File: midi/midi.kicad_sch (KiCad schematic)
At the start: 36 parts, among them J1 Conn_01x02, J2 SJ-43515TS-SMT-TR, J3 USB_C_Receptacle_USB2.0_16P, U3 MAX98357A, U4 MAX98357A, U5 CD74HC154M96, U6 ESP32-S2-SOLO

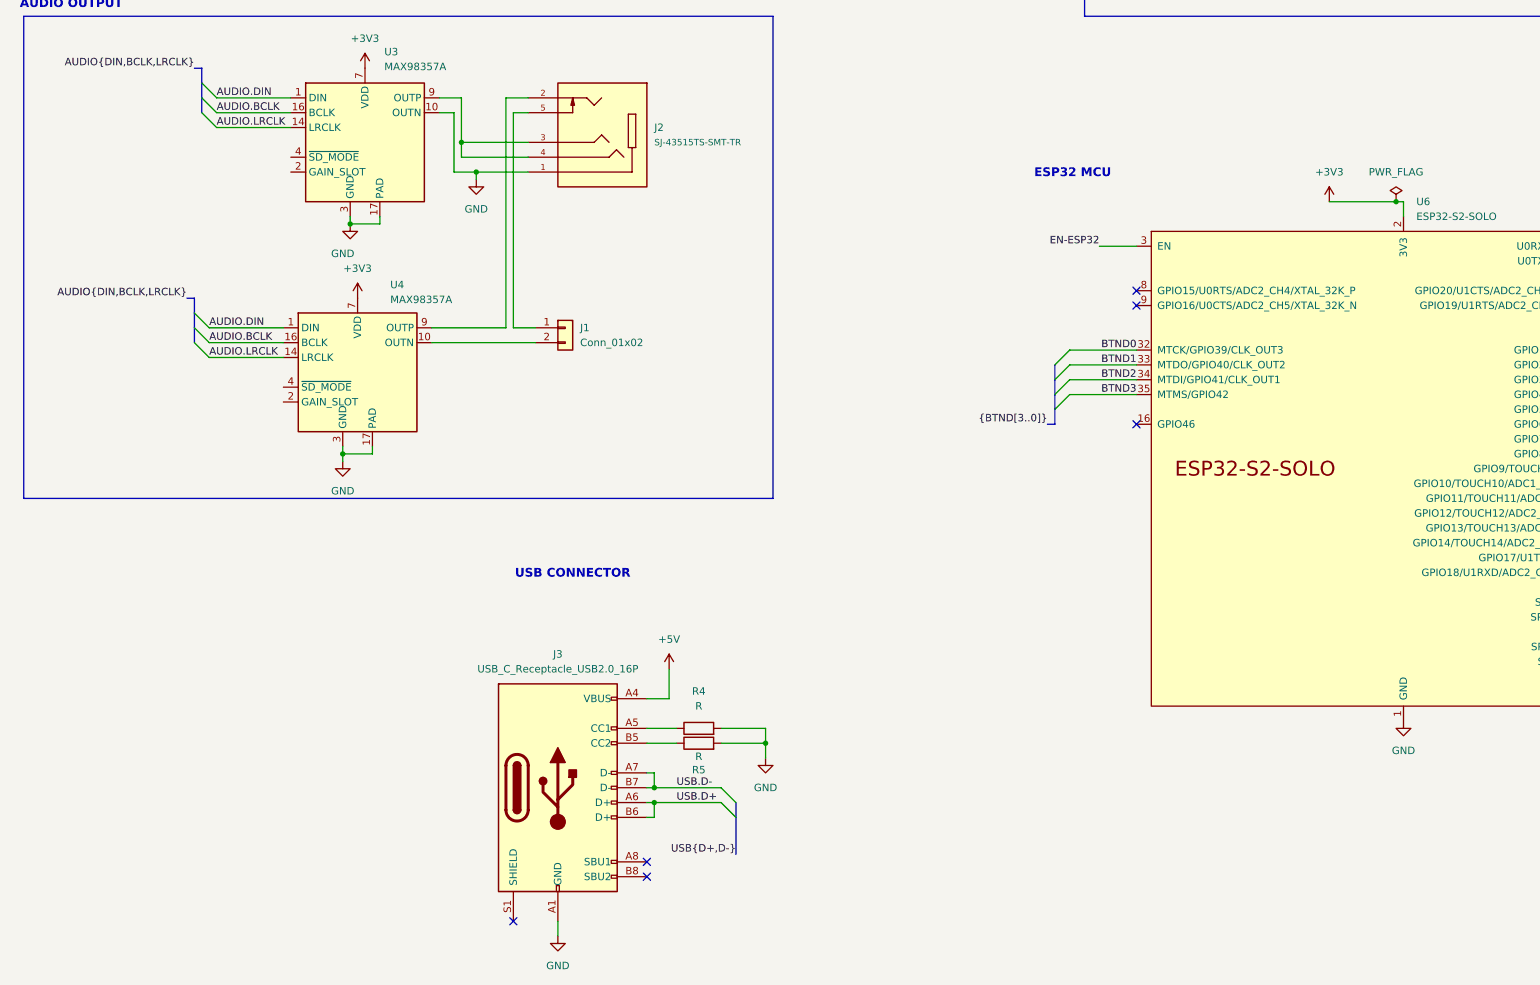
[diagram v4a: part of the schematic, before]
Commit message: new vreg
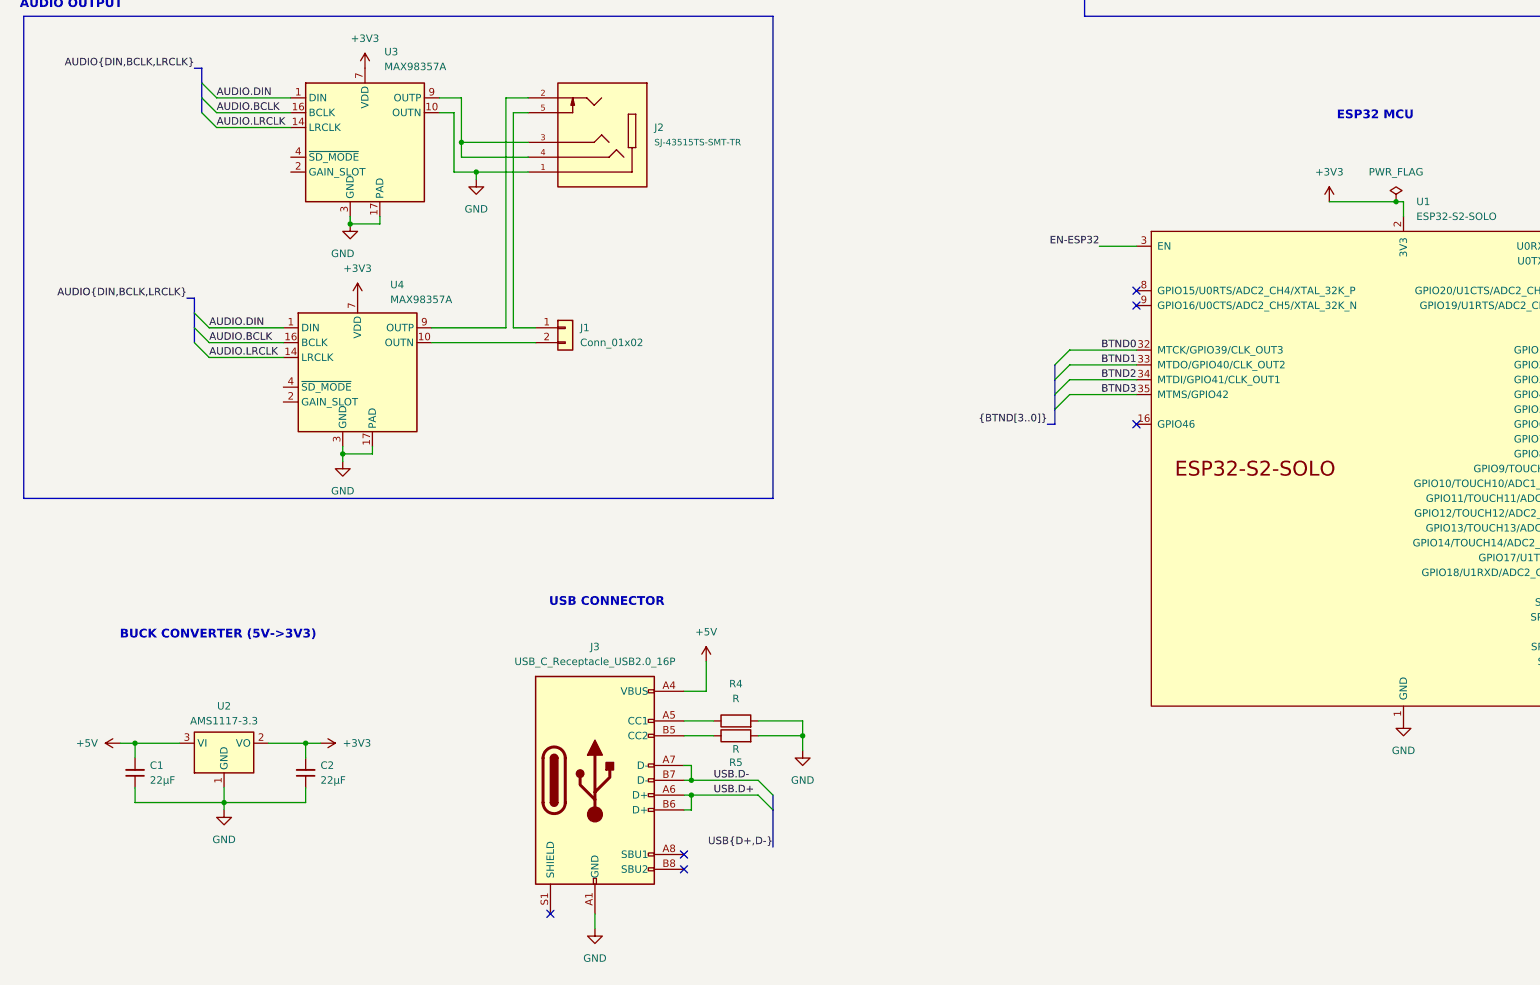
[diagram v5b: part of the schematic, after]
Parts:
- removed U6: ESP32-S2-SOLO, PCM_Espressif:ESP32-S2-SOLO, symbol PCM_Espressif:ESP32-S2-SOLO
- added C1, C2: 22µF, symbol Device:C_Small
- added U1: ESP32-S2-SOLO, PCM_Espressif:ESP32-S2-SOLO, symbol PCM_Espressif:ESP32-S2-SOLO
- added U2: AMS1117-3.3, Package_TO_SOT_SMD:SOT-223-3_TabPin2, symbol Regulator_Linear:AMS1117-3.3
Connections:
- net +3V3: now also C2.2, U1.2 (3V3), U2.2 (VO)
- net +5V: now also C1.2, U2.3 (VI)
- net AUDIO.BCLK: now also U1.11 (GPIO18/U1RXD/ADC2_CH7/DAC_2/CLK_OUT3)
- net AUDIO.DIN: now also U1.15 (GPIO3/TOUCH3/ADC1_CH2)
- net AUDIO.LRCLK: now also U1.4 (GPIO4/TOUCH4/ADC1_CH3)
- net BTND0: now also U1.32 (MTCK/GPIO39/CLK_OUT3)
- net BTND1: now also U1.33 (MTDO/GPIO40/CLK_OUT2)
- net BTND2: now also U1.34 (MTDI/GPIO41/CLK_OUT1)
- net BTND3: now also U1.35 (MTMS/GPIO42)
- net EN-ESP32: now also U1.3 (EN)
- net GND: now also C1.1, C2.1, U1.1 (GND), U1.40 (GND), U1.41 (GND), U2.1 (GND)
- net LCD.A0: now also U1.26 (GPIO45)
- net LCD.CS1: now also U1.25 (SPIIO5/GPIO34/FSPICS0)
- net LCD.RST: now also U1.23 (GPIO21)
- net LCD.SCL: now also U1.29 (SPIIO7/GPIO36/FSPICLK)
- net LCD.SI: now also U1.28 (SPIIO6/GPIO35/FSPID)
- net RV1: now also U1.39 (GPIO1/TOUCH1/ADC1_CH0)
- net RV2: now also U1.38 (GPIO2/TOUCH2/ADC1_CH1)
- net USB.D+: now also U1.14 (GPIO20/U1CTS/ADC2_CH9/CLK_OUT1/USB_D+)
- net USB.D-: now also U1.13 (GPIO19/U1RTS/ADC2_CH8/CLK_OUT2/USB_D-)
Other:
- note added: "BUCK CONVERTER (5V->3V3)"
- moved on the sheet: J3, R4, R5

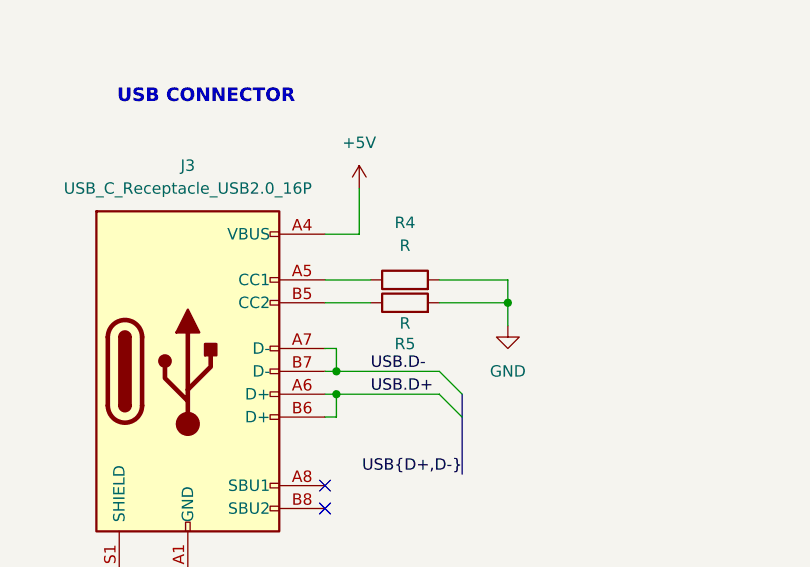
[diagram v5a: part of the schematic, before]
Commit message: assign more footprints
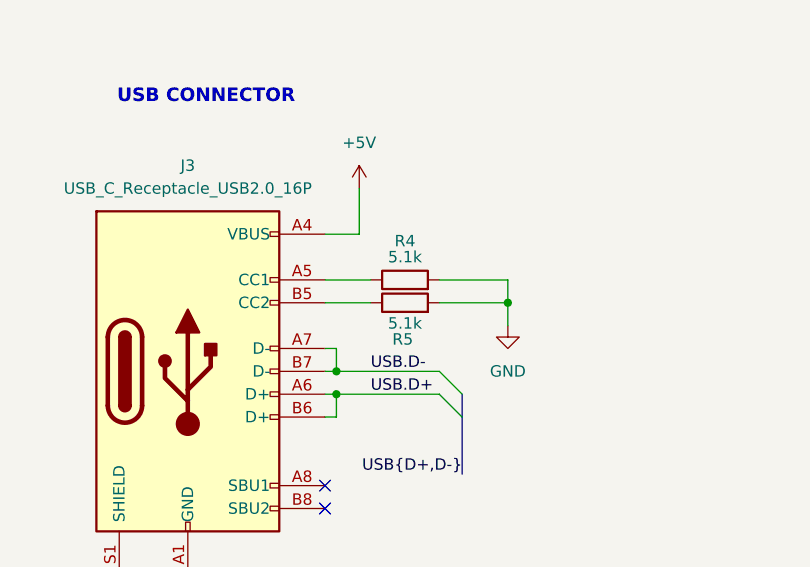
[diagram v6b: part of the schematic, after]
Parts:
- C1, C2: footprint (none) -> Capacitor_SMD:C_0805_2012Metric_Pad1.18x1.45mm_HandSolder
- R4, R5: value R -> 5.1k; footprint (none) -> Resistor_SMD:R_0805_2012Metric_Pad1.20x1.40mm_HandSolder
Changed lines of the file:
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@@
 		(on_board yes)
 		(dnp no)
-		(fields_autoplaced yes)
 		(property "Reference" "R4"
-			(at 167.64 226.06 90)
+			(at 167.64 228.092 90)
 			(effects
 				(font
@@
 			)
 		)
-		(property "Value" "R"
-			(at 167.64 228.6 90)
+		(property "Value" "5.1k"
+			(at 167.64 229.87 90)
 			(effects
 				(font
@@
 			)
 		)
-		(property "Footprint" ""
+		(property "Footprint" "Resistor_SMD:R_0805_2012Metric_Pad1.20x1.40mm_HandSolder"
 			(at 167.64 234.188 90)
 			(effects
@@
 			)
 		)
-		(property "Footprint" ""
+		(property "Footprint" "Capacitor_SMD:C_0805_2012Metric_Pad1.18x1.45mm_HandSolder"
 			(at 93.98 241.3 0)
 			(effects
@@
 			)
 		)
-		(property "Footprint" ""
+		(property "Footprint" "Capacitor_SMD:C_0805_2012Metric_Pad1.18x1.45mm_HandSolder"
 			(at 64.77 241.3 0)
 			(effects
@@
 		(dnp no)
 		(property "Reference" "R5"
-			(at 167.64 239.522 90)
+			(at 167.386 239.014 90)
 			(effects
 				(font
@@
 			)
 		)
-		(property "Value" "R"
+		(property "Value" "5.1k"
 			(at 167.64 237.236 90)
 			(effects
@@
 			)
 		)
-		(property "Footprint" ""
+		(property "Footprint" "Resistor_SMD:R_0805_2012Metric_Pad1.20x1.40mm_HandSolder"
 			(at 167.64 236.728 90)
 			(effects

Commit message: layout progress
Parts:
- removed S1, S10, S11, S12, S13, S14, S15, S16, S2, S3, S4, S5, S6, S7, S8, S9: KS-01Q-01_Obsolete, BTN_TL3301AF160QJ:TL3301AF160QJ_EWI, symbol dk_Pushbutton-Switches:KS-01Q-01_Obsolete
- removed U2: AMS1117-3.3, Package_TO_SOT_SMD:SOT-223-3_TabPin2, symbol Regulator_Linear:AMS1117-3.3
- added C13, C14, C3: .1µF, Capacitor_SMD:C_0603_1608Metric_Pad1.08x0.95mm_HandSolder, symbol Device:C_Small
- added C4: 1µF, Capacitor_SMD:C_0603_1608Metric_Pad1.08x0.95mm_HandSolder, symbol Device:C_Small
- added L1: 1µH, Inductor_SMD:L_0805_2012Metric_Pad1.15x1.40mm_HandSolder, symbol Device:L
- added R1, R2: 634k, Resistor_SMD:R_0603_1608Metric_Pad0.98x0.95mm_HandSolder, symbol Device:R
- added R3: 10k, Resistor_SMD:R_0603_1608Metric_Pad0.98x0.95mm_HandSolder, symbol Device:R
- added SW1: Reset, Button_Switch_THT:SW_PUSH_6mm_H5mm, symbol Switch:SW_Push
- added SW10, SW11, SW12, SW13, SW14, SW15, SW16, SW17, SW18, SW3, SW4, SW5, SW6, SW7, SW8, SW9: SW_Push, Button_Switch_THT:SW_PUSH_6mm_H5mm, symbol Switch:SW_Push
- added SW2: Boot, Button_Switch_THT:SW_PUSH_6mm_H5mm, symbol Switch:SW_Push
- added U2: SC189ZSKTRT, SC189ZSKTRT:SOT23-5-SC189_SEM, symbol SC189ZSKTRT:SC189ZSKTRT
- C1: footprint Capacitor_SMD:C_0805_2012Metric_Pad1.18x1.45mm_HandSolder -> Capacitor_SMD:C_0603_1608Metric_Pad1.08x0.95mm_HandSolder
- C2: value 22µF -> 10µF; footprint Capacitor_SMD:C_0805_2012Metric_Pad1.18x1.45mm_HandSolder -> Capacitor_SMD:C_0603_1608Metric_Pad1.08x0.95mm_HandSolder
- J3: footprint (none) -> USB4105-GF-A:GCT_USB4105-GF-A
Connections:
- net +3V3: now also C1.1, U3.2 (GAIN_SLOT), U4.2 (GAIN_SLOT), C13.2, C4.2, L1.2, R1.1, R2.1, R3.1, U2.4 (VOUT); no longer C2.2
- net +5V: now also C2.1, J3.A4_B9 (VBUS), U2.1 (VIN), U2.3 (EN); no longer C1.2, J3.A4 (VBUS)
- net GND: now also C1.2, C2.2, J3.A1_B12 (GND), C13.1, C14.1, C3.1, C4.1, SW1.1, SW10.2, SW11.2, SW12.2, SW13.2, SW14.2, SW15.2, SW16.2, SW17.2, SW18.2, SW2.2, SW3.2, SW4.2, SW5.2, SW6.2, SW7.2, SW8.2, SW9.2, U2.2 (GND); no longer C1.1, C2.1, J3.A1 (GND)
- net LCD.A0: now also LCD1.15 (A0)
- net S1: now also SW3.1
- net S10: now also SW12.1
- net S11: now also SW13.1
- net S12: now also SW14.1
- net S13: now also SW15.1
- net S14: now also SW16.1
- net S15: now also SW17.1
- net S16: now also SW18.1
- net S2: now also SW4.1
- net S3: now also SW5.1
- net S4: now also SW6.1
- net S5: now also SW7.1
- net S6: now also SW8.1
- net S7: now also SW9.1
- net S8: now also SW10.1
- net S9: now also SW11.1
- net at U3.4 (~{SD_MODE}): now also R1.2
- net at U4.4 (~{SD_MODE}): now also R2.2
- net at U1.27 (GPIO0): now also C14.2, SW2.1
- net EN-ESP32: no longer names the net of U1.3 (EN)
- net EN-ESP32: now also C3.2, R3.2, SW1.2
- new net: L1.1, U2.5 (LX)
- no-connect marks 28 -> 26
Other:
- note added: "ESP32 MODULE"
- note added: "VOLTAGE REGULATOR"
- note removed: "BUCK CONVERTER (5V->3V3)"
- note removed: "ESP32 MCU"
- moved on the sheet: J3, R4, R5, RV1, RV2, U1, U4, U5

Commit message: slight ERC fixes for gnd/power in
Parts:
- U2: footprint SC189ZSKTRT:SOT23-5-SC189_SEM -> SOT23-5-SC189_SEM
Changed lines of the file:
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@@
 		)
 	)
+	(label "S1"
+		(at 265.43 83.82 0)
+		(fields_autoplaced yes)
+		(effects
+			(font
+				(size 1.27 1.27)
+			)
+			(justify left bottom)
+		)
+	)
 	(label "BTND3"
 		(at 231.14 76.2 0)
@@
 	(label "LCD.A0"
 		(at 82.55 68.58 0)
+		(fields_autoplaced yes)
 		(effects
 			(font
@@
 		)
 	)
-	(label "S1"
-		(at 265.43 83.82 0)
-		(fields_autoplaced yes)
-		(effects
-			(font
-				(size 1.27 1.27)
-			)
-			(justify left bottom)
-		)
-	)
 	(label "BTND0"
 		(at 260.35 170.18 180)
@@
 			)
 		)
-		(property "Footprint" "SC189ZSKTRT:SOT23-5-SC189_SEM"
+		(property "Footprint" "SOT23-5-SC189_SEM"
 			(at 69.85 236.22 0)
 			(effects
